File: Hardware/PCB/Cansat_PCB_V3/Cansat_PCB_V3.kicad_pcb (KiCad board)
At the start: 6 copper layers, 31.8 x 25.4 mm, 101 parts, among them IC1 Alim STM Baro GPS IMU, IC2 Alim LoRa, J1 Lecteur SD, J10 Connecteur IHM, J2 Connecteur Batterie, J3 Connecteur STLINK, J4 Connecteur Moteur, J5 Connecteur TOF, J6 Connecteur GPS, J7 Connecteur LoRa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

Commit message: importing new readme
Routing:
- net (no net): vias 1 -> 0

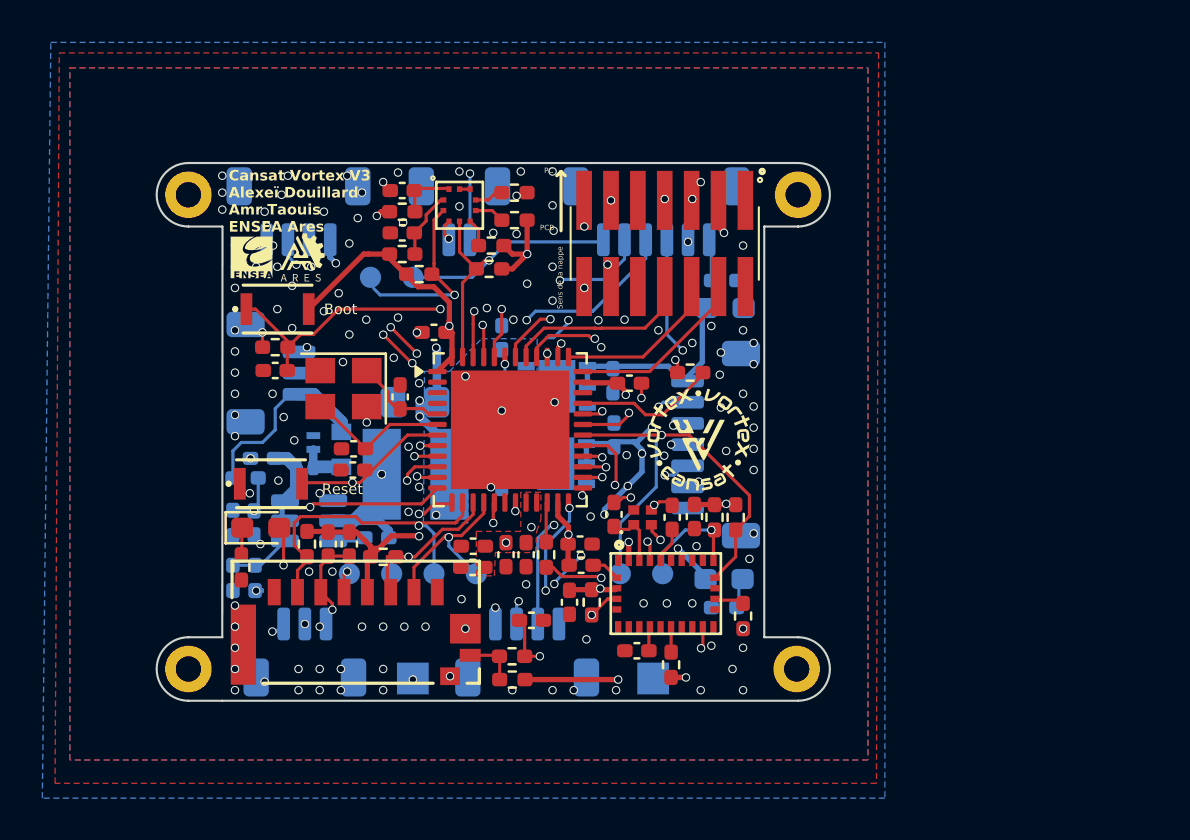
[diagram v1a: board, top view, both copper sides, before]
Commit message: added the UART2 for the camera as well as M2 holes
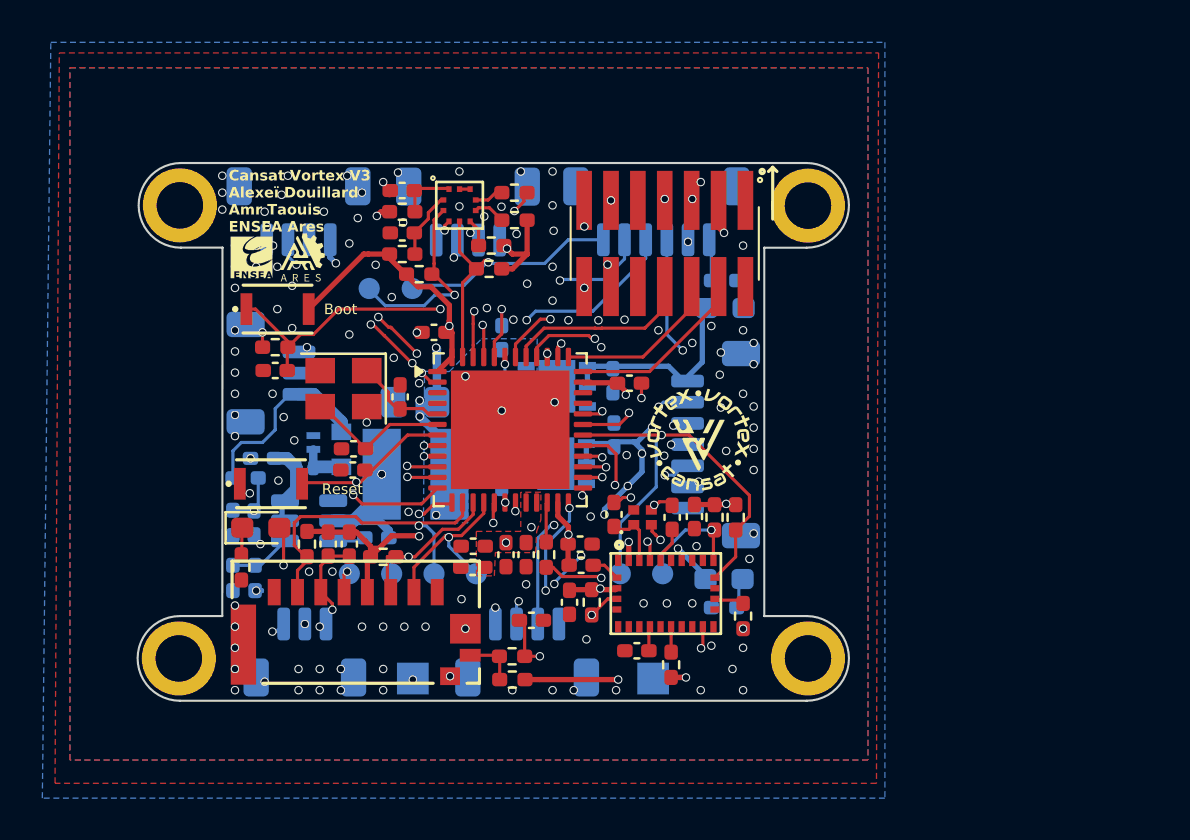
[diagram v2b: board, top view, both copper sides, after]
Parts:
- removed J8: Connecteur Camera, Connector_JST:JST_SH_BM02B-SRSS-TB_1x02-1MP_P1.00mm_Vertical
- removed R20: 10k, Resistor_SMD:R_0402_1005Metric_Pad0.72x0.64mm_HandSolder
- added J9: Connecteur Camera, Connector_JST:JST_SH_BM04B-SRSS-TB_1x04-1MP_P1.00mm_Vertical, B.Cu at (148.0, 90.4)
- H1, H2, H3, H4: footprint footprints:mountinghole1.2mm -> MountingHole:MountingHole_2.2mm_M2_ISO7380_Pad
- moved G*** 0.93 mm to (152.1, 94.2)
- moved H2 0.73 mm to (164.1, 111.5)
- moved H1 0.69 mm to (164.1, 90.1)
- moved H4 0.67 mm to (134.3, 111.5)
- moved H3 0.64 mm to (134.4, 90.1)
- moved TP1 0.53 mm to (143.3, 94.0)
- moved TP2 0.53 mm to (145.4, 94.0)
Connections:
- C24 pad 2: ADC1_IN3_VBAT -> ADC1_IN12_VBAT
- J10 pad 4: EXTI3_BTN -> EXTI13_BTN
- R19 pad 1: ADC1_IN3_VBAT -> ADC1_IN12_VBAT
- R21 pad 2: ADC1_IN3_VBAT -> ADC1_IN12_VBAT
- U2 pad 10: ADC1_IN3_VBAT -> USART2_TX_CAM
- U2 pad 11: EXTI3_BTN -> USART2_RX_CAM
- U2 pad 18: unconnected-(U2-PB1-Pad18) -> ADC1_IN12_VBAT
- U2 pad 2: unconnected-(U2-PC13-Pad2) -> EXTI13_BTN
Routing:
- net USART2_RX_CAM: track 0.00 -> 21.1 mm, vias 0 -> 2
- net EXTI3_BTN: track 20.6 -> 0.00 mm, vias 2 -> 0
- net ADC1_IN12_VBAT: track 0.00 -> 19.3 mm, vias 0 -> 2
- net CAM_EN: track 19.0 -> 0.00 mm, vias 2 -> 0
- net USART2_TX_CAM: track 0.00 -> 19.0 mm, vias 0 -> 2
- net EXTI13_BTN: track 0.00 -> 14.5 mm, vias 0 -> 2
- net ADC1_IN3_VBAT: track 13.5 -> 0.00 mm, vias 2 -> 0
- net Net-(U2-PA11): track 6.77 -> 0.00 mm
- net EXTI_BARO: track 25.7 -> 22.4 mm
- net GND: track 20.7 -> 18.9 mm, vias 145 -> 138
- net IMU_BOOT: track 14.2 -> 13.3 mm
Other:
- board size 31.8 x 25.4 mm -> 33.6 x 25.4 mm
- board text removed: "PC"
- board text removed: "PCB"
- board text removed: "Sens de la nappe"

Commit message: added marking to the testpoints
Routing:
- net Net-(U5-SW): vias 2 -> 0
- net GND: vias 138 -> 139
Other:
- board text added: "cs"
- board text added: "miso"
- board text added: "mosi"
- board text added: "scl"
- board text added: "sda"
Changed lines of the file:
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@@
 		)
 	)
-	(gr_text "+5V"
-		(at 146.2 111.2 0)
+	(gr_text "scl"
+		(at 143.0344 108.9612 0)
 		(layer "B.SilkS")
 		(effects
 			(font
 				(size 0.5 0.5)
-				(thickness 0.125)
-			)
-			(justify left bottom mirror)
-		)
-	)
-	(gr_text "+3.3V"
-		(at 157.9 111.1 0)
+				(thickness 0.1)
+				(bold yes)
+			)
+			(justify left bottom mirror)
+		)
+	)
+	(gr_text "sda"
+		(at 143.9996 93.2132 0)
 		(layer "B.SilkS")
 		(effects
 			(font
 				(size 0.5 0.5)
-				(thickness 0.125)
+				(thickness 0.1)
+				(bold yes)
+			)
+			(justify left bottom mirror)
+		)
+	)
+	(gr_text "mosi"
+		(at 145.3204 108.9612 0)
+		(layer "B.SilkS")
+		(effects
+			(font
+				(size 0.5 0.5)
+				(thickness 0.1)
+				(bold yes)
+			)
+			(justify left bottom mirror)
+		)
+	)
+	(gr_text "scl"
+		(at 145.9808 93.2132 0)
+		(layer "B.SilkS")
+		(effects
+			(font
+				(size 0.5 0.5)
+				(thickness 0.1)
+				(bold yes)
+			)
+			(justify left bottom mirror)
+		)
+	)
+	(gr_text "miso"
+		(at 147.4032 108.9612 0)
+		(layer "B.SilkS")
+		(effects
+			(font
+				(size 0.5 0.5)
+				(thickness 0.1)
+				(bold yes)
+			)
+			(justify left bottom mirror)
+		)
+	)
+	(gr_text "cs"
+		(at 148.8764 108.9612 0)
+		(layer "B.SilkS")
+		(effects
+			(font
+				(size 0.5 0.5)
+				(thickness 0.1)
+				(bold yes)
+			)
+			(justify left bottom mirror)
+		)
+	)
+	(gr_text "scl"
+		(at 155.7852 109.012 0)
+		(layer "B.SilkS")
+		(effects
+			(font
+				(size 0.5 0.5)
+				(thickness 0.1)
+				(bold yes)
+			)
+			(justify left bottom mirror)
+		)
+	)
+	(gr_text "sda"
+		(at 157.9188 109.012 0)
+		(layer "B.SilkS")
+		(effects
+			(font
+				(size 0.5 0.5)
+				(thickness 0.1)
+				(bold yes)
 			)
 			(justify left bottom mirror)
@@
 	)
 	(gr_text "GPS"
-		(at 141.5 93.9 0)
+		(at 141.358 93.8228 0)
 		(layer "B.SilkS")
 		(effects
@@
 	)
 	(gr_text "Mot\n"
-		(at 141.6 108.8 0)
+		(at 141.5104 108.8088 0)
 		(layer "B.SilkS")
 		(effects
@@
 	)
 	(gr_text "SD"
-		(at 145.9 109.4 0)
+		(at 146.0824 106.5228 0)
 		(layer "B.SilkS")
 		(effects
@@
 		)
 	)
-	(gr_text "Cam"
-		(at 149.3844 93.7212 0)
+	(gr_text "+5V"
+		(at 146.7936 111.298 0)
 		(layer "B.SilkS")
 		(effects
@@
 		)
 	)
-	(gr_text "TOF"
-		(at 151.8 108.7 0)
+	(gr_text "Cam"
+		(at 149.3336 93.772 0)
 		(layer "B.SilkS")
 		(effects
@@
 		)
 	)
-	(gr_text "IMU"
-		(at 157.3 109.4 0)
+	(gr_text "TOF"
+		(at 151.8736 108.7072 0)
 		(layer "B.SilkS")
 		(effects
@@
 		)
 	)
+	(gr_text "IMU"
+		(at 157.3092 106.5228 0)
+		(layer "B.SilkS")
+		(effects
+			(font
+				(size 0.8 0.8)
+				(thickness 0.15)
+				(bold yes)
+			)
+			(justify left bottom mirror)
+		)
+	)
 	(gr_text "IHM"
-		(at 158.1728 93.8736 0)
+		(at 158.3252 93.7212 0)
+		(layer "B.SilkS")
+		(effects
+			(font
+				(size 0.8 0.8)
+				(thickness 0.15)
+				(bold yes)
+			)
+			(justify left bottom mirror)
+		)
+	)
+	(gr_text "+3.3V"
+		(at 158.9856 111.298 0)
 		(layer "B.SilkS")
 		(effects
@@
 	)
 	(segment
+		(start 143.22345 99.6059)
+		(end 143.22345 100.353698)
+		(width 0.15)
+		(layer "F.Cu")
+		(net 2)
+	)
+	(segment
 		(start 155.32 103.9)
 		(end 154.95 104.27)
@@
 	)
 	(segment
-		(start 143.22345 99.6059)
-		(end 143.22345 100.353698)
-		(width 0.15)
-		(layer "F.Cu")
-		(net 2)
-	)
-	(segment
 		(start 157.3 89.8)
 		(end 157.3 89.865)
@@
 		(keep_end_layers yes)
 		(zone_layer_connections "In1.Cu" "In2.Cu" "In4.Cu")
+		(net 2)
+	)
+	(via
+		(at 145.4728 103.7796)
+		(size 0.4)
+		(drill 0.3)
+		(layers "F.Cu" "B.Cu")
+		(free yes)
 		(net 2)
 	)
@@
 		(net 11)
 	)
-	(via
-		(at 143.93 102.8)
-		(size 0.4)
-		(drill 0.3)
-		(layers "F.Cu" "B.Cu")
-		(net 12)
-	)
-	(via
-		(at 143.93 102.8)
-		(size 0.4)
-		(drill 0.3)
-		(layers "F.Cu" "B.Cu")
-		(net 12)
-	)
-	(segment
+	(segment

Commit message: mega big readme update for the mechanical and wind tunnel parts
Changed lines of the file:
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@@
 			(drillshape 0)
 			(scaleselection 1)
-			(outputdirectory "/home/alexei/Bureau/Gerber_Cansat/")
+			(outputdirectory "/home/alexei/Bureau/Gerber_Cansat_V3/")
 		)
 	)
@@
 	)
 	(segment
-		(start 144.356471 95.85646)
-		(end 144.4 95.899989)
-		(width 0.15)
-		(layer "F.Cu")
-		(net 24)
-	)
-	(segment
-		(start 145.59 97.09)
-		(end 145.59 97.1)
+		(start 143.7716 95.375)
+		(end 143.875011 95.375)
 		(width 0.15)
 		(layer "F.Cu")
@@
 	)
 	(segment
-		(start 144.25306 95.85646)
-		(end 144.356471 95.85646)
+		(start 144.4 95.9)
+		(end 145.59 97.09)
 		(width 0.15)
 		(layer "F.Cu")
@@
 	)
 	(segment
-		(start 143.7716 95.375)
-		(end 144.25306 95.85646)
+		(start 143.875011 95.375)
+		(end 144.4 95.899989)
 		(width 0.15)
 		(layer "F.Cu")
@@
 	)
 	(segment
-		(start 144.4 95.9)
-		(end 145.59 97.09)
+		(start 144.4 95.899989)
+		(end 144.4 95.9)
 		(width 0.15)
 		(layer "F.Cu")
@@
 	)
 	(segment
-		(start 144.4 95.899989)
-		(end 144.4 95.9)
+		(start 145.59 97.09)
+		(end 145.59 97.1)
 		(width 0.15)
 		(layer "F.Cu")
@@
 	)
 	(segment
-		(start 143.4154 95.7278)
-		(end 143.520693 95.7278)
+		(start 143.520693 95.7278)
+		(end 145.344534 97.551641)
 		(width 0.15)
 		(layer "F.Cu")
@@
 	)
 	(segment
-		(start 144.059956 96.259956)
-		(end 145.351641 97.551641)
-		(width 0.15)
-		(layer "F.Cu")
-		(net 25)
-	)
-	(segment
 		(start 149.25 96.525)
 		(end 149.25 97.2625)
@@
 	)
 	(segment
-		(start 144.052849 96.259956)
-		(end 144.059956 96.259956)
+		(start 149.6 95)
+		(end 149.6 96.175)
 		(width 0.15)
 		(layer "F.Cu")
@@
 	)
 	(segment
-		(start 145.351641 97.551641)
+		(start 145.344534 97.551641)
 		(end 145.37547 97.551641)
 		(width 0.15)
@@
 	)
 	(segment
-		(start 149.6 95)
-		(end 149.6 96.175)
+		(start 143.4154 95.7278)
+		(end 143.520693 95.7278)
 		(width 0.15)
 		(layer "F.Cu")
@@
 		(net 25)
 	)
-	(segment
-		(start 143.520693 95.7278)
-		(end 144.052849 96.259956)
-		(width 0.15)
-		(layer "F.Cu")
-		(net 25)
-	)
 	(via
 		(at 149.6 95)
@@
 	)
 	(segment
-		(start 155.4 92.630043)
+		(start 155.4 92.7348)
 		(end 155.4 91.825)
 		(width 0.15)
@@
 	)
 	(segment
-		(start 154.430043 93.6)
-		(end 155.4 92.630043)
+		(start 154.5348 93.6)
+		(end 155.4 92.7348)
 		(width 0.15)
 		(layer "B.Cu")
@@
 	)
 	(segment
-		(start 152.35 93.65)
-		(end 152.4 93.6)
+		(start 147.375 94.330262)
+		(end 146.438538 94.330262)
 		(width 0.15)
 		(layer "B.Cu")
@@
 	)
 	(segment
-		(start 147.375 94.330262)
-		(end 146.438538 94.330262)
+		(start 152.4 93.6)
+		(end 154.5348 93.6)
 		(width 0.15)
 		(layer "B.Cu")
@@
 	)
 	(segment
-		(start 152.4 93.6)
-		(end 154.430043 93.6)
+		(start 152.35 93.65)
+		(end 152.4 93.6)
 		(width 0.15)
 		(layer "B.Cu")
@@
 	)
 	(via
-		(at 152.084834 107.984834)
+		(at 152.112507 108.011093)
 		(size 0.4)
 		(drill 0.3)
@@
 	)
 	(segment
-		(start 152.084834 107.922835)
-		(end 153.35 106.657669)
+		(start 152.084834 107.98342)
+		(end 152.084834 107.922835)
 		(width 0.15)
 		(layer "B.Cu")
@@
 	)
 	(segment
-		(start 152.084834 107.984834)
-		(end 152.084834 107.922835)
+		(start 152.084834 107.922835)
+		(end 153.35 106.657669)
 		(width 0.15)
 		(layer "B.Cu")
@@
 	)
 	(segment
-		(start 138.764589 110.232295)
-		(end 138.942705 110.232295)
+		(start 152.112507 108.011093)
+		(end 152.084834 107.98342)
 		(width 0.15)
 		(layer "B.Cu")
@@
 	)
 	(segment
-		(start 138.764589 110.419557)
-		(end 139.721808 111.376776)
+		(start 138.764589 110.232295)
+		(end 138.942705 110.232295)
 		(width 0.15)
-		(layer "In2.Cu")
+		(layer "B.Cu")
 		(net 41)
 	)
 	(segment
-		(start 152.084834 108.615166)
-		(end 152.084834 107.984834)
+		(start 154.95 103.310799)
+		(end 154.95 103.45)
 		(width 0.15)
 		(layer "In2.Cu")
@@
 	)
 	(segment
-		(start 154.95 103.310799)
-		(end 154.95 103.45)
+		(start 139.721808 111.376776)
+		(end 138.764589 110.419557)
 		(width 0.15)
 		(layer "In2.Cu")
@@
 	)
 	(segment
-		(start 138.764589 110.232295)
-		(end 138.764589 110.419557)
+		(start 149.323224 111.376776)
+		(end 139.721808 111.376776)
 		(width 0.15)
 		(layer "In2.Cu")
@@
 	)
 	(segment
-		(start 139.721808 111.376776)
-		(end 149.323224 111.376776)
+		(start 138.764589 110.419557)
+		(end 138.764589 110.232295)
 		(width 0.15)
 		(layer "In2.Cu")
@@
 	)
 	(segment
-		(start 149.323224 111.376776)
+		(start 152.084834 108.615166)
+		(end 149.323224 111.376776)
+		(width 0.15)
+		(layer "In2.Cu")
+		(net 41)
+	)
+	(segment
+		(start 152.084834 108.038766)
 		(end 152.084834 108.615166)
 		(width 0.15)
@@
 	)
 	(segment
+		(start 152.112507 108.011093)
+		(end 152.084834 108.038766)
+		(width 0.15)
+		(layer "In2.Cu")
+		(net 41)
+	)
+	(segment
 		(start 152.8 104.1875)
 		(end 152.75 104.1375)
@@
 	(segment
 		(start 157.15 100.95)
-		(end 156.9 101.2)
+		(end 156.8012 101.2988)
 		(width 0.15)
 		(layer "B.Cu")
@@
 	)
 	(segment
-		(start 155.2 105.1)
-		(end 155.2 107.5)
+		(start 156.8012 103.4988)
+		(end 155.2 105.1)
 		(width 0.15)
 		(layer "B.Cu")
@@
 	)
 	(segment
-		(start 156.9 101.2)
-		(end 156.9 103.4)
+		(start 155.2 105.1)
+		(end 155.2 107.5)
 		(width 0.15)
 		(layer "B.Cu")
@@
 	)
 	(segment
-		(start 156.9 103.4)
-		(end 155.2 105.1)
+		(start 156.8012 101.2988)
+		(end 156.8012 103.4988)
 		(width 0.15)
 		(layer "B.Cu")
